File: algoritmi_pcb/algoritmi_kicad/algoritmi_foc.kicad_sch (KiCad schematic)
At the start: 35 parts, among them IC1 MA710GQ-Z, IC2 AP2114HA-3.3TRG1, J2 53261-0371, J3 SMM-115-02-S-D-LC-K-TR, U1 TMC6300-LA-T

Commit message: changes
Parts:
- removed C6: 1uF, CAPC1608X90N, symbol SamacSys_Parts:CL10A105KA8NNNC
- removed IC1: MA710GQ-Z, QFN50P300X300X100-17N-D, symbol SamacSys_Parts:MA710GQ-Z
- removed J3: SMM-115-02-S-D-LC-K-TR, SMM11502SDLCKTR, symbol SamacSys_Parts:SMM-115-02-S-D-LC-K-TR
- removed MSW1, MSW2, MSW3, MSW4: ~, solder_pads:solder_pads_4mm_3, symbol solder_pad:solder_pad_4mm_3
- removed R11, R12, R13, R14: 300R, ERJUP3, symbol SamacSys_Parts:ERJ-UP3F3000V
- added J3: SMM-110-02-H-D-K-TR, SMM-110-02-XX-D-K-TR, symbol SamacSys_Parts:SMM-110-02-H-D-K-TR
- C1, C2, C3, C4: footprint CAPC1608X90N -> Capacitor_SMD:C_0201_0603Metric
- C5, C9: footprint CAPC2012X145N -> Capacitor_SMD:C_0805_2012Metric
- C7, C8: footprint CAPC2012X140N -> Capacitor_SMD:C_0805_2012Metric
- D1, D2: footprint LEDM1620X150N -> LED_SMD:LED_0603_1608Metric
- IC2: footprint SOT230P700X180-4N -> Package_TO_SOT_SMD:SOT-223-3_TabPin2
- R1, R2: value 300R -> 300; footprint ERJUP3 -> Resistor_SMD:R_0201_0603Metric
- R10, R5, R6, R7, R8, R9: footprint RESC1608X55N -> Resistor_SMD:R_0201_0603Metric
- R3, R4: footprint RESC3216X70N -> Resistor_SMD:R_1206_3216Metric
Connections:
- net +5V: now also J3.18, J3.20
- net GND: now also J3.14, J3.16, J3.7
- net LCD_BL: now also J3.12
- net LCD_CLOCK: now also J3.4
- net LCD_CS: now also J3.6
- net LCD_DATA_IN: now also J3.2
- net LCD_DC: now also J3.8
- net LCD_RESET: now also J3.10
- net UH: now also J3.19
- net UL: now also J3.13
- net U_OUT: now also J2.3; no longer J2.1
- net VH: now also J3.17
- net VL: now also J3.11
- net WH: now also J3.15
- net WL: now also J3.9
- net W_OUT: now also J2.1; no longer J2.3
- new net E_CLK: J3.3
- new net E_CSN: J3.5
- new net E_DO: J3.1
- no-connect marks 9 -> 3
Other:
- note added: "Must keep track of this orientation. (W-1, V-2, U-3)"
- note added: "This circuit was based on the instructions given by the datasheet and the adaptations made by the creator of NANOFOC, Karl Binaris"
- note removed: "HALL SENSOR - MA710GQ-Z"
- note removed: "MICROSWITCH CIRCUIT"
- moved on the sheet: C7, C8, IC2

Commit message: updates
updates to the pcb
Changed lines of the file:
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@@
+	(wire
+		(pts
+			(xy 29.21 135.89) (xy 31.75 135.89)
+		)
+		(stroke
+			(width 0)
+			(type default)
+		)
+	)
 	(wire
 		(pts
@@
 				(hide yes)
 			)
+		)
+	)
+	(global_label "VS"
+		(shape output)
+		(at 29.21 135.89 180)
+		(fields_autoplaced yes)
+		(effects
+			(font
+				(size 1.27 1.27)
+			)
+			(justify right)
+		)
+		(property "Intersheetrefs" "${INTERSHEET_REFS}"
+			(at 23.9267 135.89 0)
+			(effects
+				(font
+					(size 1.27 1.27)
+				)
+				(justify right)
+				(hide yes)
+			)

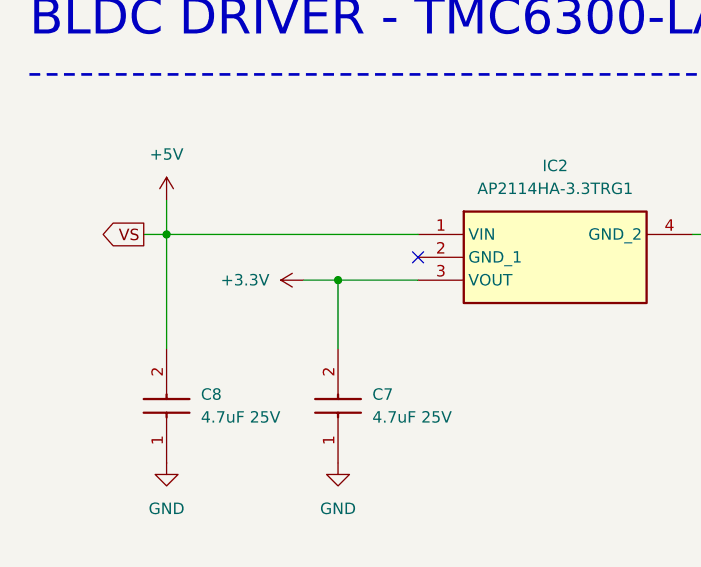
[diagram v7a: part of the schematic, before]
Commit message: finished base pcb
in the last meeting with professor, we decided to separate the smartknob into 3 pcb's, one that contains the encoder and the motor, the other that contains the connectors and motor driver, and another one that contains the lcd
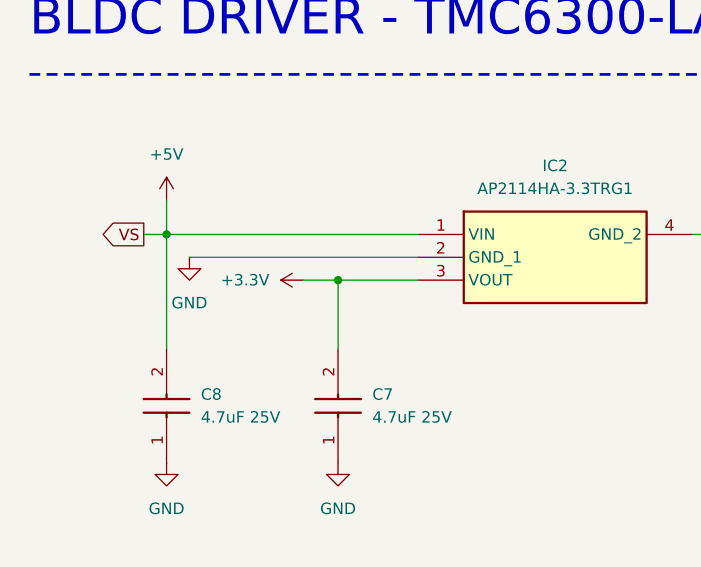
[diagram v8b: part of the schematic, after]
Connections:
- net GND: now also IC2.2 (GND_1)
- no-connect marks 3 -> 2
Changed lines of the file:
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@@
-	)
-	(no_connect
-		(at 59.69 138.43)
 	)
 	(no_connect
@@
 		(pts
 			(xy 173.99 53.34) (xy 139.7 53.34)
+		)
+		(stroke
+			(width 0)
+			(type default)
+		)
+	)
+	(wire
+		(pts
+			(xy 34.29 138.43) (xy 59.69 138.43)
 		)
 		(stroke
@@
 					(unit 1)
 				)
+			)
+		)
+	)
+	(symbol
+		(lib_name "GND_1")
+		(lib_id "power:GND")
+		(at 34.29 138.43 0)
+		(unit 1)
+		(exclude_from_sim no)
+		(in_bom yes)
+		(on_board yes)
+		(dnp no)
+		(fields_autoplaced yes)
+		(property "Reference" "#PWR014"
+			(at 34.29 144.78 0)
+			(effects
+				(font
+					(size 1.27 1.27)
+				)
+				(hide yes)
+			)
+		)
+		(property "Value" "GND"
+			(at 34.29 143.51 0)
+			(effects
+				(font
+					(size 1.27 1.27)
+				)
+			)
+		)
+		(property "Footprint" ""
+			(at 34.29 138.43 0)
+			(effects
+				(font
+					(size 1.27 1.27)
+				)
+				(hide yes)
+			)
+		)
+		(property "Datasheet" ""
+			(at 34.29 138.43 0)
+			(effects
+				(font
+					(size 1.27 1.27)
+				)
+				(hide yes)
+			)
+		)
+		(property "Description" "Power symbol creates a global label with name \"GND\" , ground"
+			(at 34.29 138.43 0)
+			(effects
+				(font
+					(size 1.27 1.27)
+				)
+				(hide yes)
+			)
+		)
+		(pin "1"
+		)
+		(instances
+			(project ""
+				(path "/dc7944a0-8802-4fe0-accc-4447b8be9489"
+					(reference "#PWR014")
+					(unit 1)
+				)
